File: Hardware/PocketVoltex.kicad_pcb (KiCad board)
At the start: 2 copper layers, 168 x 109.2 mm, 75 parts, among them J1 Programming header, J2 USB_C_Receptacle, SW1 MX socket, SW2 MX socket, SW3 MX socket, SW4 MX socket, SW5 MX socket, SW6 MX socket, SW7 MX socket, SW8 SW_Push, U1 ATMEGA16U2-AU, X1 16MHz

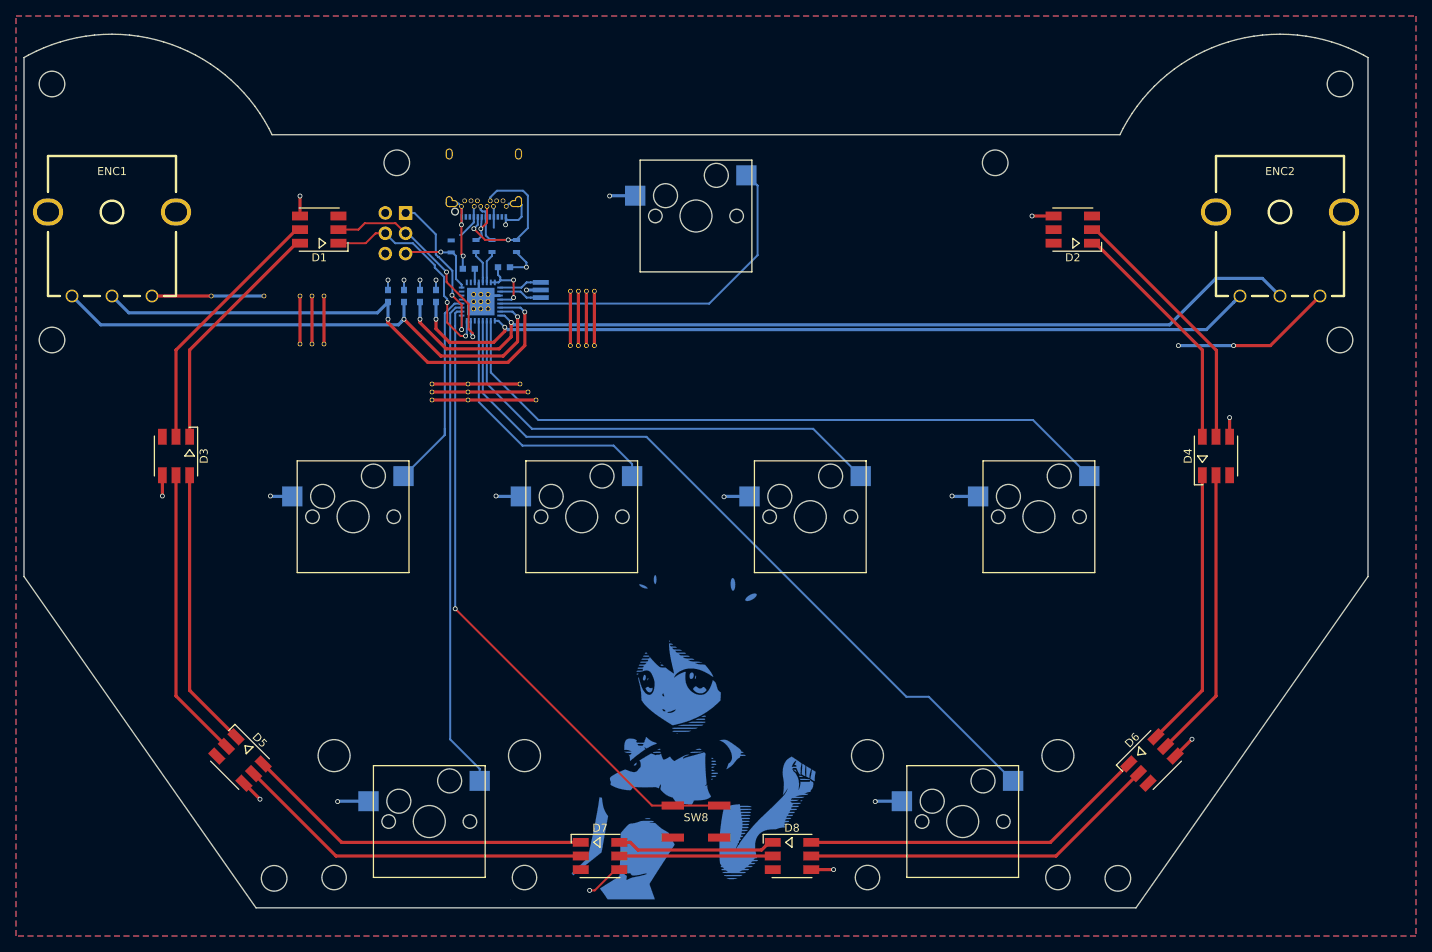
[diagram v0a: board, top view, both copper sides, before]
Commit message: rev7b - Updated layout to 4 layers
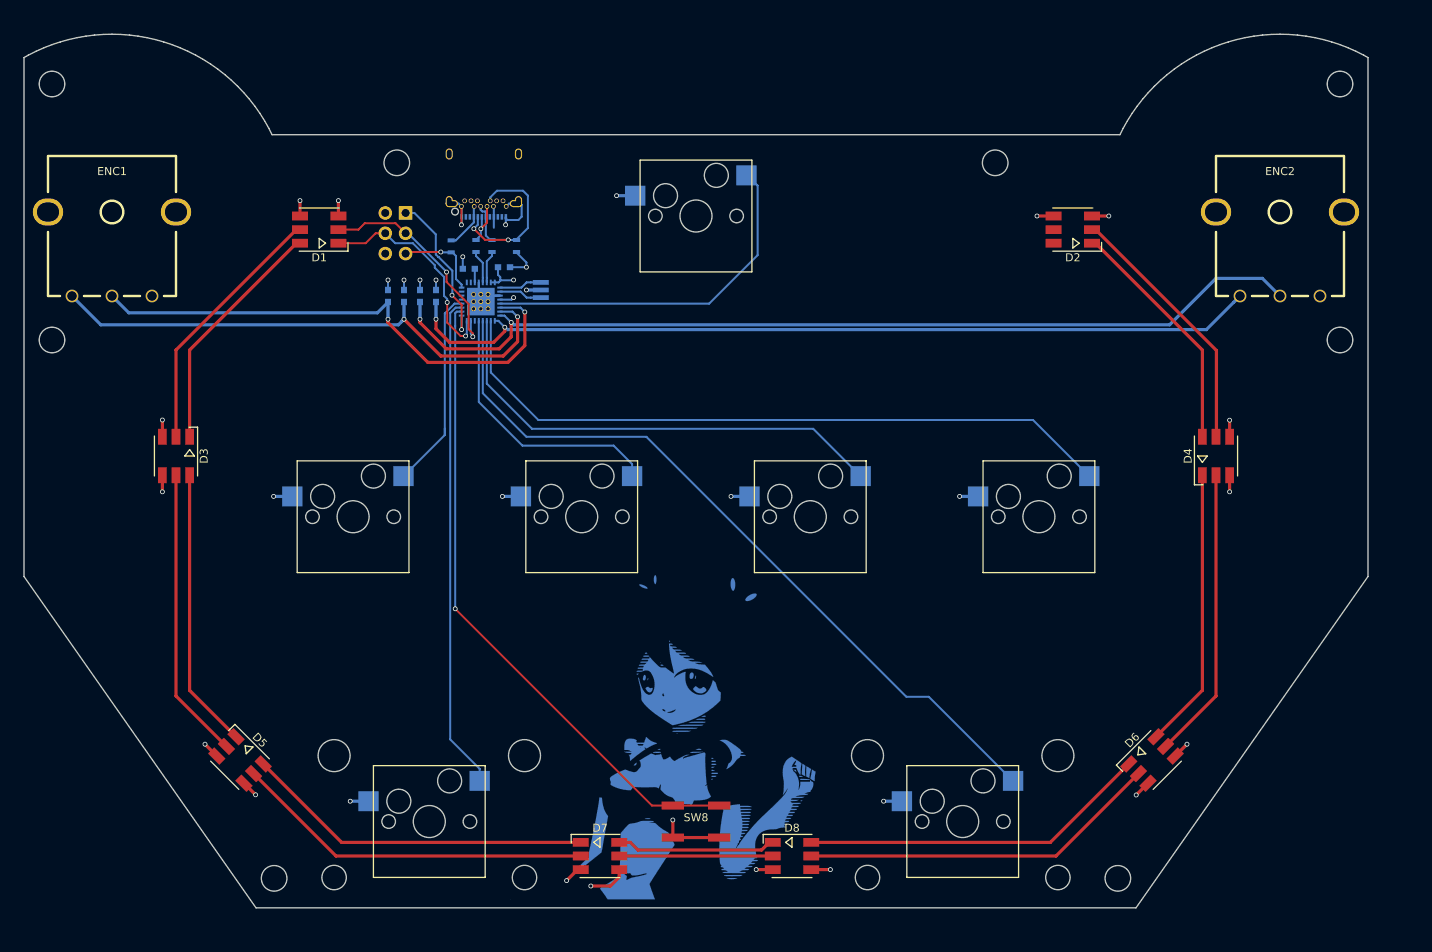
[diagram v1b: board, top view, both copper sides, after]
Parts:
- removed the REF** at (122.2, 87.0)
- removed the REF** at (122.2, 88.0)
- removed the REF** at (122.2, 89.0)
- removed the REF** at (133.2, 87.0)
- removed the REF** at (134.2, 88.0)
- removed the REF** at (135.2, 89.0)
- removed the REF** at (94.6, 76.0)
- removed the REF** at (101.2, 76.0)
- removed the REF** at (139.5, 82.2)
- removed the REF** at (140.5, 82.2)
- removed the REF** at (141.5, 82.2)
- removed the REF** at (142.5, 82.2)
- removed the REF** at (142.5, 75.4)
- removed the REF** at (141.5, 75.4)
- removed the REF** at (140.5, 75.4)
- removed the REF** at (139.5, 75.4)
- removed the REF** at (126.7, 87.0)
- removed the REF** at (126.7, 88.0)
- removed the REF** at (126.7, 89.0)
- removed the REF** at (105.7, 76.0)
- removed the REF** at (107.2, 76.0)
- removed the REF** at (108.7, 76.0)
- removed the REF** at (105.7, 82.0)
- removed the REF** at (107.2, 82.0)
- removed the REF** at (108.7, 82.0)
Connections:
- D2 pad 5: Net-(D2-Pad5) -> unconnected-(D2-Pad5)
- D2 pad 6: Net-(D2-Pad6) -> unconnected-(D2-Pad6)
- ENC1 pad 2: (no net) -> GND
- ENC2 pad 2: (no net) -> GND
- J2 pad A8: Net-(J2-PadA8) -> unconnected-(J2-PadA8)
- J2 pad B8: Net-(J2-PadB8) -> unconnected-(J2-PadB8)
- U1 pad 14: Net-(U1-Pad14) -> unconnected-(U1-Pad14)
- U1 pad 21: Net-(U1-Pad21) -> unconnected-(U1-Pad21)
- U1 pad 22: Net-(U1-Pad22) -> unconnected-(U1-Pad22)
- U1 pad 23: Net-(U1-Pad23) -> unconnected-(U1-Pad23)
- U1 pad 25: Net-(U1-Pad25) -> unconnected-(U1-Pad25)
- U1 pad 26: Net-(U1-Pad26) -> unconnected-(U1-Pad26)
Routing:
- net VCC: track 120.8 -> 34.7 mm
- net (no net): track 20.3 -> 0.00 mm, vias 2 -> 0
- net GND: vias 16 -> 25
- added copper zone on In1.Cu, net GND
- added copper zone on In2.Cu, net VCC
- removed copper zone on F.Cu, net GND
- removed copper zone on B.Cu, net VCC
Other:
- copper layers 2 -> 4
- net class Default removed
- board text added: "2022 Rev 7b"
- board text removed: "2021 Rev 7a"
